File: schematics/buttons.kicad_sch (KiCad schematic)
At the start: 21 parts, among them SW2 SW_SPST, SW3 SW_SPST, SW4 SW_SPST, SW5 SW_SPST, SW6 SW_SPST, SW7 SW_SPST, SW8 SW_SPST, SW9 SW_SPST, U2 ADS1115IDGS

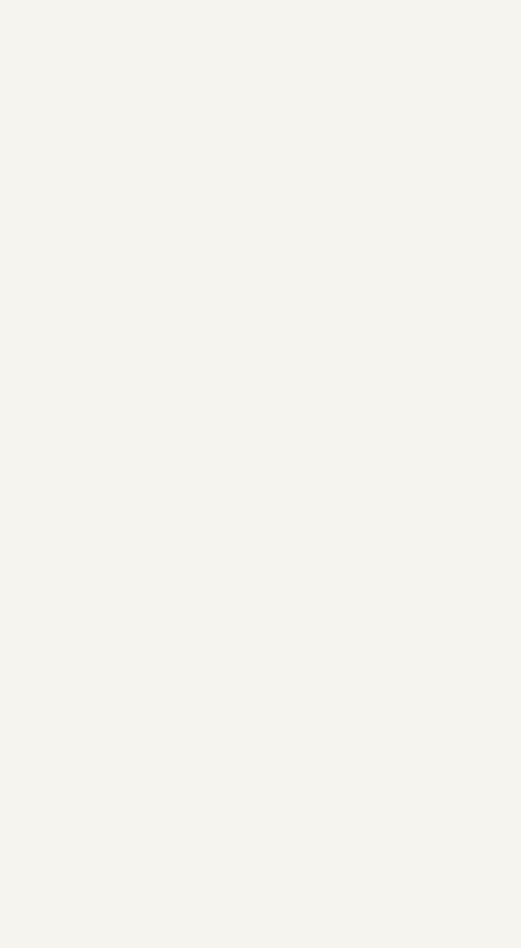
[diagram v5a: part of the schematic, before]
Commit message: Added LEDs and improved decals
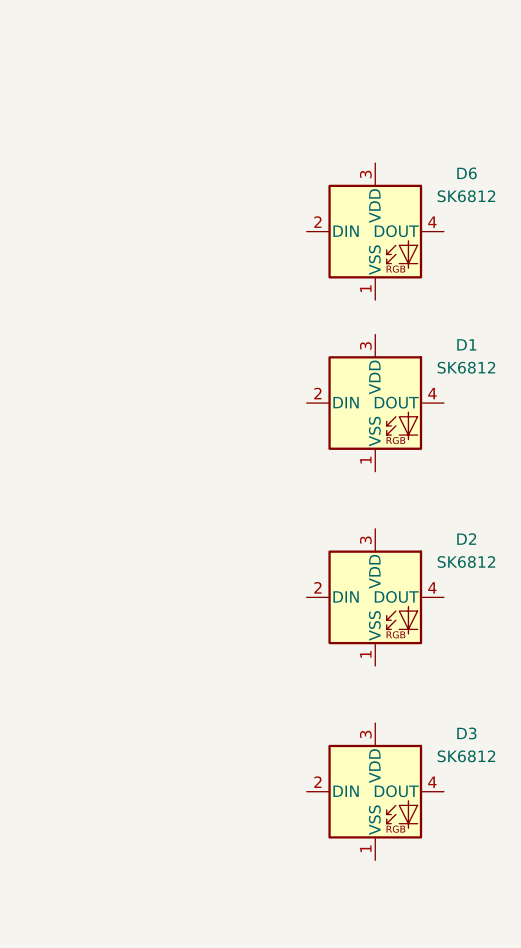
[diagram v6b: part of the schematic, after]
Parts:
- added D1, D2, D3, D6: SK6812, LED_SMD:LED_SK6812_PLCC4_5.0x5.0mm_P3.2mm, symbol LED:SK6812

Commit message: Update pcb
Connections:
- net +3.3V: now also D1.3 (VDD), D2.3 (VDD), D3.3 (VDD), D6.3 (VDD)
- net GND: now also D1.1 (VSS), D2.1 (VSS), D3.1 (VSS), D6.1 (VSS)
- net at D3.2 (DIN): now also D2.4 (DOUT)
- net at D3.4 (DOUT): now also D6.2 (DIN)
- net at D2.2 (DIN): now also D1.4 (DOUT)
- net LED_MCU: now reaches D1.2 (DIN)
- no-connect marks 0 -> 1
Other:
- moved on the sheet: D1, D2, D3, D6

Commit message: Update power traces
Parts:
- SW2, SW3, SW4, SW5, SW6, SW7, SW8, SW9: footprint PCM_Switch_Keyboard_Cherry_MX:SW_Cherry_MX_PCB_1.00u -> PCM_Switch_Keyboard_Cherry_MX:SW_Cherry_MX_PCB
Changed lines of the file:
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@@
 			)
 		)
-		(property "Footprint" "PCM_Switch_Keyboard_Cherry_MX:SW_Cherry_MX_PCB_1.00u"
+		(property "Footprint" "PCM_Switch_Keyboard_Cherry_MX:SW_Cherry_MX_PCB"
 			(at 78.74 87.63 0)
 			(effects
@@
 			)
 		)
-		(property "Footprint" "PCM_Switch_Keyboard_Cherry_MX:SW_Cherry_MX_PCB_1.00u"
+		(property "Footprint" "PCM_Switch_Keyboard_Cherry_MX:SW_Cherry_MX_PCB"
 			(at 96.52 87.63 0)
 			(effects
@@
 			)
 		)
-		(property "Footprint" "PCM_Switch_Keyboard_Cherry_MX:SW_Cherry_MX_PCB_1.00u"
+		(property "Footprint" "PCM_Switch_Keyboard_Cherry_MX:SW_Cherry_MX_PCB"
 			(at 78.74 60.96 0)
 			(effects
@@
 			)
 		)
-		(property "Footprint" "PCM_Switch_Keyboard_Cherry_MX:SW_Cherry_MX_PCB_1.00u"
+		(property "Footprint" "PCM_Switch_Keyboard_Cherry_MX:SW_Cherry_MX_PCB"
 			(at 78.74 77.47 0)
 			(effects
@@
 			)
 		)
-		(property "Footprint" "PCM_Switch_Keyboard_Cherry_MX:SW_Cherry_MX_PCB_1.00u"
+		(property "Footprint" "PCM_Switch_Keyboard_Cherry_MX:SW_Cherry_MX_PCB"
 			(at 96.52 60.96 0)
 			(effects
@@
 			)
 		)
-		(property "Footprint" "PCM_Switch_Keyboard_Cherry_MX:SW_Cherry_MX_PCB_1.00u"
+		(property "Footprint" "PCM_Switch_Keyboard_Cherry_MX:SW_Cherry_MX_PCB"
 			(at 78.74 69.85 0)
 			(effects
@@
 			)
 		)
-		(property "Footprint" "PCM_Switch_Keyboard_Cherry_MX:SW_Cherry_MX_PCB_1.00u"
+		(property "Footprint" "PCM_Switch_Keyboard_Cherry_MX:SW_Cherry_MX_PCB"
 			(at 96.52 69.85 0)
 			(effects
@@
 			)
 		)
-		(property "Footprint" "PCM_Switch_Keyboard_Cherry_MX:SW_Cherry_MX_PCB_1.00u"
+		(property "Footprint" "PCM_Switch_Keyboard_Cherry_MX:SW_Cherry_MX_PCB"
 			(at 96.52 77.47 0)
 			(effects
